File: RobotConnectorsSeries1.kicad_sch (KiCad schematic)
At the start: 8 parts

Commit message: v0.3 prototype
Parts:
- S1-J7: FT Rotation Offset 0 -> 90; LCSC Part # C400369 -> C505075
- S1-J9: now not fitted; now left out of the parts list
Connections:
- net BMC_GN renamed BMC_SPI_MISO
- net BMC_YW renamed BMC_SPI_CLK
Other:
- note added: "Looks like cables on PWR switch get connected wrong by Series-I design. Exchange Pin5 with Pin14 would look more logic to me."
- note removed: "--------- DESIGN FAULTS -------- 1. S1-J2 is to tight to USB. Unplugging difficult 2. S1-J2/S1-J3 is to tight. Unplugging difficult"
- note removed: "Looks like cables on PWR switch get connected wrong. Exchange Pin5 with Pin14 would look more logic to me."
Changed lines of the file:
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@@
 	(title_block
 		(title "OpenMower SABO Mainboard for Series I & II")
-		(date "2025-05-22")
-		(rev "v0.2")
+		(date "2025-10-05")
+		(rev "v0.3")
 		(company "Apeheanger <joerg@ebeling.ws> for OpenMower")
 		(comment 1 "This design is licensed under CC BY-NC 4.0")
@@
 		)
 	)
-	(text "Looks like cables on PWR switch\nget connected wrong.\nExchange Pin5 with Pin14\nwould look more logic to me."
+	(text "Looks like cables on PWR switch\nget connected wrong by Series-I design.\nExchange Pin5 with Pin14 would\nlook more logic to me."
 		(exclude_from_sim no)
 		(at 123.952 44.196 0)
@@
 		)
 	)
-	(text "--------- DESIGN FAULTS --------\n\n1. S1-J2 is to tight to USB. Unplugging difficult\n2. S1-J2/S1-J3 is to tight. Unplugging difficult"
-		(exclude_from_sim no)
-		(at 91.44 22.606 0)
-		(effects
-			(font
-				(size 1.778 1.778)
-				(thickness 0.254)
-				(bold yes)
-				(color 255 0 0 1)
-			)
-			(justify left)
-		)
-	)
 	(text "W"
 		(exclude_from_sim no)
@@
 		)
 	)
-	(hierarchical_label "BMC_GN"
-		(shape bidirectional)
-		(at 86.36 38.1 0)
-		(effects
-			(font
-				(size 1.27 1.27)
-			)
-			(justify left)
-		)
-	)
 	(hierarchical_label "UI_~{CON}"
 		(shape input)
@@
 		)
 	)
-	(hierarchical_label "HALL1_5V"
+	(hierarchical_label "BMC_SPI_CLK"
 		(shape input)
+		(at 86.36 35.56 0)
+		(effects
+			(font
+				(size 1.27 1.27)
+			)
+			(justify left)
+		)
+		(property "CableColor" "Yellow"
+			(at 77.47 34.544 0)
+			(effects
+				(font
+					(size 1.27 1.27)
+					(italic yes)
+				)
+				(justify left)
+			)
+		)
+	)
+	(hierarchical_label "HALL1_5V"
+		(shape output)
 		(at 271.78 68.58 0)
 		(effects
@@
 		)
 	)
+	(hierarchical_label "BMC_SPI_MISO"
+		(shape output)
+		(at 86.36 38.1 0)
+		(effects
+			(font
+				(size 1.27 1.27)
+			)
+			(justify left)
+		)
+		(property "CableColor" "Green"
+			(at 77.978 37.084 0)
+			(effects
+				(font
+					(size 1.27 1.27)
+					(italic yes)
+				)
+				(justify left)
+			)
+		)
+	)
 	(hierarchical_label "SPK_PLUS"
 		(shape output)
@@
 	)
 	(hierarchical_label "HALL2_5V"
-		(shape input)
+		(shape output)
 		(at 210.82 24.13 0)
 		(effects
@@
 	)
 	(hierarchical_label "HALL3_5V"
-		(shape input)
+		(shape output)
 		(at 267.97 34.29 0)
 		(effects
@@
 		)
 	)
-	(hierarchical_label "BMC_YW"
-		(shape bidirectional)
-		(at 86.36 35.56 0)
-		(effects
-			(font
-				(size 1.27 1.27)
-			)
-			(justify left)
-		)
-	)
 	(hierarchical_label "MC_HALL_SENSOR{U V W}"
 		(shape output)
@@
 	)
 	(hierarchical_label "HALL0_5V"
-		(shape input)
+		(shape output)
 		(at 271.78 91.44 0)
 		(effects
@@
 			)
 		)
+		(property "Alternative" ""
+			(at 69.85 146.05 0)
+			(effects
+				(font
+					(size 1.27 1.27)
+				)
+				(hide yes)
+			)
+		)
+		(property "LCSC" ""
+			(at 69.85 146.05 0)
+			(effects
+				(font
+					(size 1.27 1.27)
+				)
+				(hide yes)
+			)
+		)
 		(pin "1"
 		)
@@
 			)
 		)
+		(property "Alternative" ""
+			(at 69.85 80.01 0)
+			(effects
+				(font
+					(size 1.27 1.27)
+				)
+				(hide yes)
+			)
+		)
+		(property "LCSC" ""
+			(at 69.85 80.01 0)
+			(effects
+				(font
+					(size 1.27 1.27)
+				)
+				(hide yes)
+			)
+		)
 		(pin "1"
 		)
@@
 		(unit 1)
 		(exclude_from_sim no)
-		(in_bom yes)
+		(in_bom no)
 		(on_board yes)
-		(dnp no)
+		(dnp yes)
 		(property "Reference" "S1-J9"
 			(at 245.364 57.404 0)
@@
 			)
 		)
+		(property "Alternative" ""
+			(at 243.84 78.74 0)
+			(effects
+				(font
+					(size 1.27 1.27)
+				)
+				(hide yes)
+			)
+		)
+		(property "LCSC" ""
+			(at 243.84 78.74 0)
+			(effects
+				(font
+					(size 1.27 1.27)
+				)
+				(hide yes)
+			)
+		)
 		(pin "24"
 		)
@@
 			)
 		)
+		(property "Alternative" ""
+			(at 191.77 105.41 0)
+			(effects
+				(font
+					(size 1.27 1.27)
+				)
+				(hide yes)
+			)
+		)
+		(property "LCSC" ""
+			(at 191.77 105.41 0)
+			(effects
+				(font
+					(size 1.27 1.27)
+				)
+				(hide yes)
+			)
+		)
 		(pin "4"
 		)
@@
 			)
 		)
-		(property "FT Rotation Offset" "0"
+		(property "FT Rotation Offset" "90"
+			(at 243.84 31.75 0)
+			(effects
+				(font
+					(size 1.27 1.27)
+				)
+				(hide yes)
+			)
+		)
+		(property "LCSC Part #" "C505075"
+			(at 243.84 31.75 0)
+			(effects
+				(font
+					(size 1.27 1.27)
+				)
+			)
+		)
+		(property "Alternative" ""
 			(at 243.84 31.75 0)
 			(effects
@@
 			)
 		)
-		(property "LCSC Part #" "C400369"
+		(property "LCSC" ""
 			(at 243.84 31.75 0)
 			(effects
@@
 					(size 1.27 1.27)
 				)
+				(hide yes)
 			)
 		)
@@
 			)
 		)
+		(property "Alternative" ""
+			(at 191.77 44.45 0)
+			(effects
+				(font
+					(size 1.27 1.27)
+				)
+				(hide yes)
+			)
+		)
+		(property "LCSC" ""
+			(at 191.77 44.45 0)
+			(effects
+				(font
+					(size 1.27 1.27)
+				)
+				(hide yes)
+			)
+		)
 		(pin "4"
 		)
@@
 			)
 		)
+		(property "Alternative" ""
+			(at 69.85 114.3 0)
+			(effects
+				(font
+					(size 1.27 1.27)
+				)
+				(hide yes)
+			)
+		)
+		(property "LCSC" ""
+			(at 69.85 114.3 0)
+			(effects
+				(font
+					(size 1.27 1.27)
+				)
+				(hide yes)
+			)
+		)
 		(pin "1"
 		)
@@
 			(at 69.85 43.18 0)
 			(effects
+				(font
+					(size 1.27 1.27)
+				)
+				(hide yes)
+			)
+		)
+		(property "Alternative" ""
+			(at 69.85 43.18 0)
+			(effects
+				(font
+					(size 1.27 1.27)
+				)
+				(hide yes)
+			)
+		)
+		(property "LCSC" ""
+			(at 69.85 43.18 0)
+			(effects

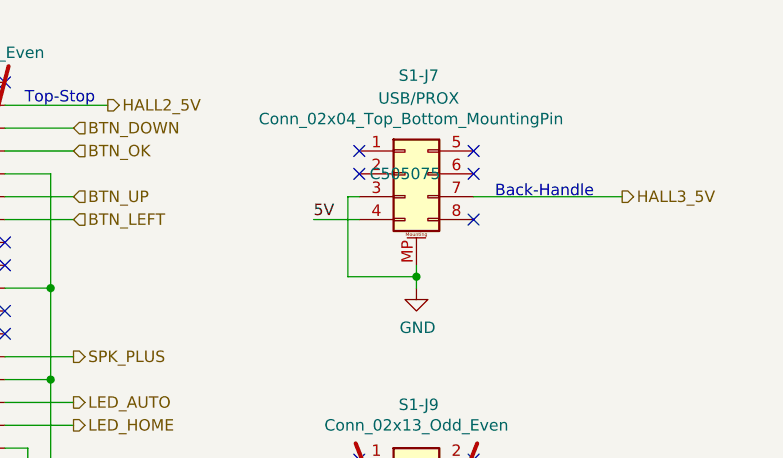
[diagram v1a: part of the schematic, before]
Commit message: ✨ feat(schematic): add rework notes and component updates
- add detailed rework instructions for series-i and series-ii boards
- add component replacement notes for capacitors
- add design fault notes for current sense circuit
- add voltage level issue explanation for led control
- add rc filter calculation note for agpio2
- add todo notes for bms spi routing and lcd ce line

🔧 chore(schematic): update component properties and connectivity

- update wire connections for agpio2 net
- update junction positions and wire routing

⚙️  chore(project): update erc settings

- set undefined netclass to error in electrical rules
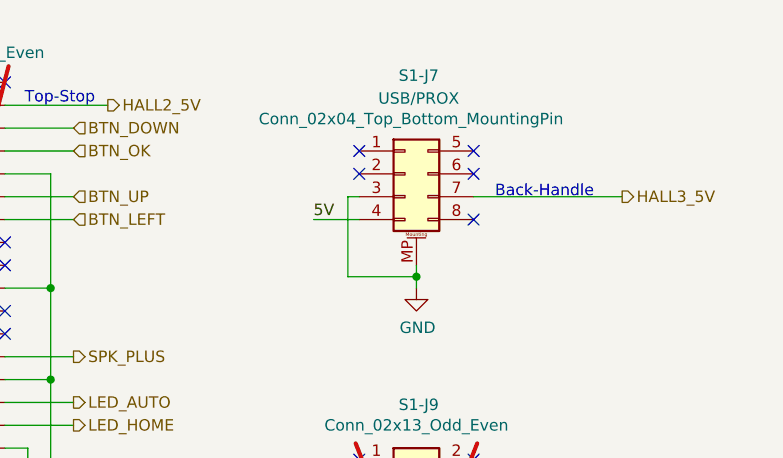
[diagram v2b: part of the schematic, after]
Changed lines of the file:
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@@
 					(size 1.27 1.27)
 				)
+				(hide yes)
 			)
 		)
